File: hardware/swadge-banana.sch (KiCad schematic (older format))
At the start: 54 parts, among them J1 USB_B_Micro, SW1 SW_SPDT, SW2 4-1437565-2, SW3 4-1437565-2, SW4 4-1437565-2, U1 GS321-TR, U2 AP1117-33, U4 ESP-13-WROOM-02D, U5 BUS_PCIexpress, U6 DISP_OLED_UG-2864HSWEG01, U9 QMA6981

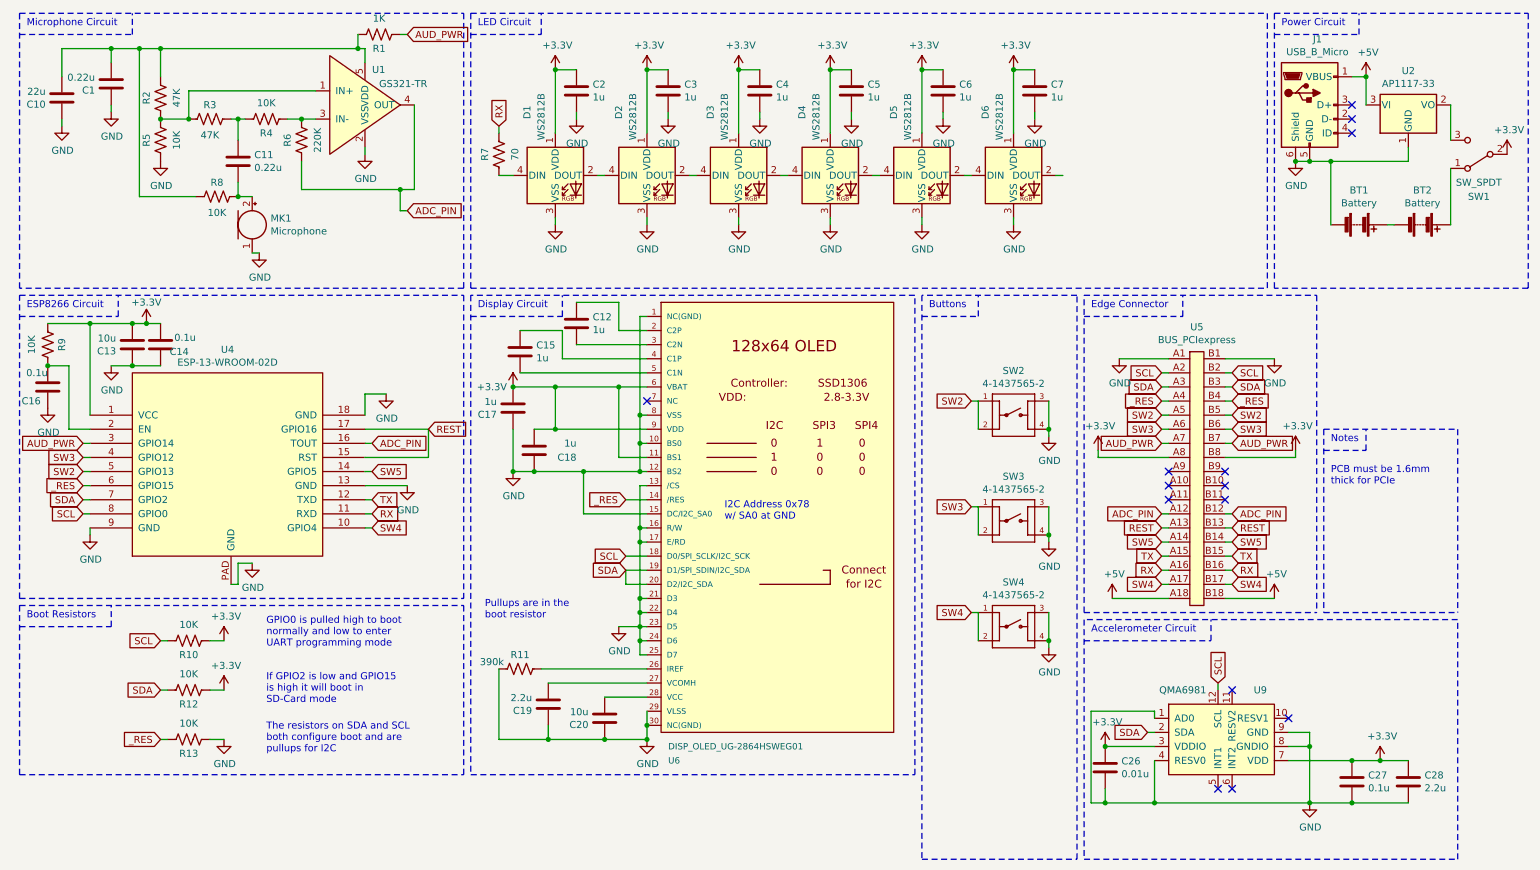
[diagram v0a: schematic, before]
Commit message: Reworked banana, started laying it out
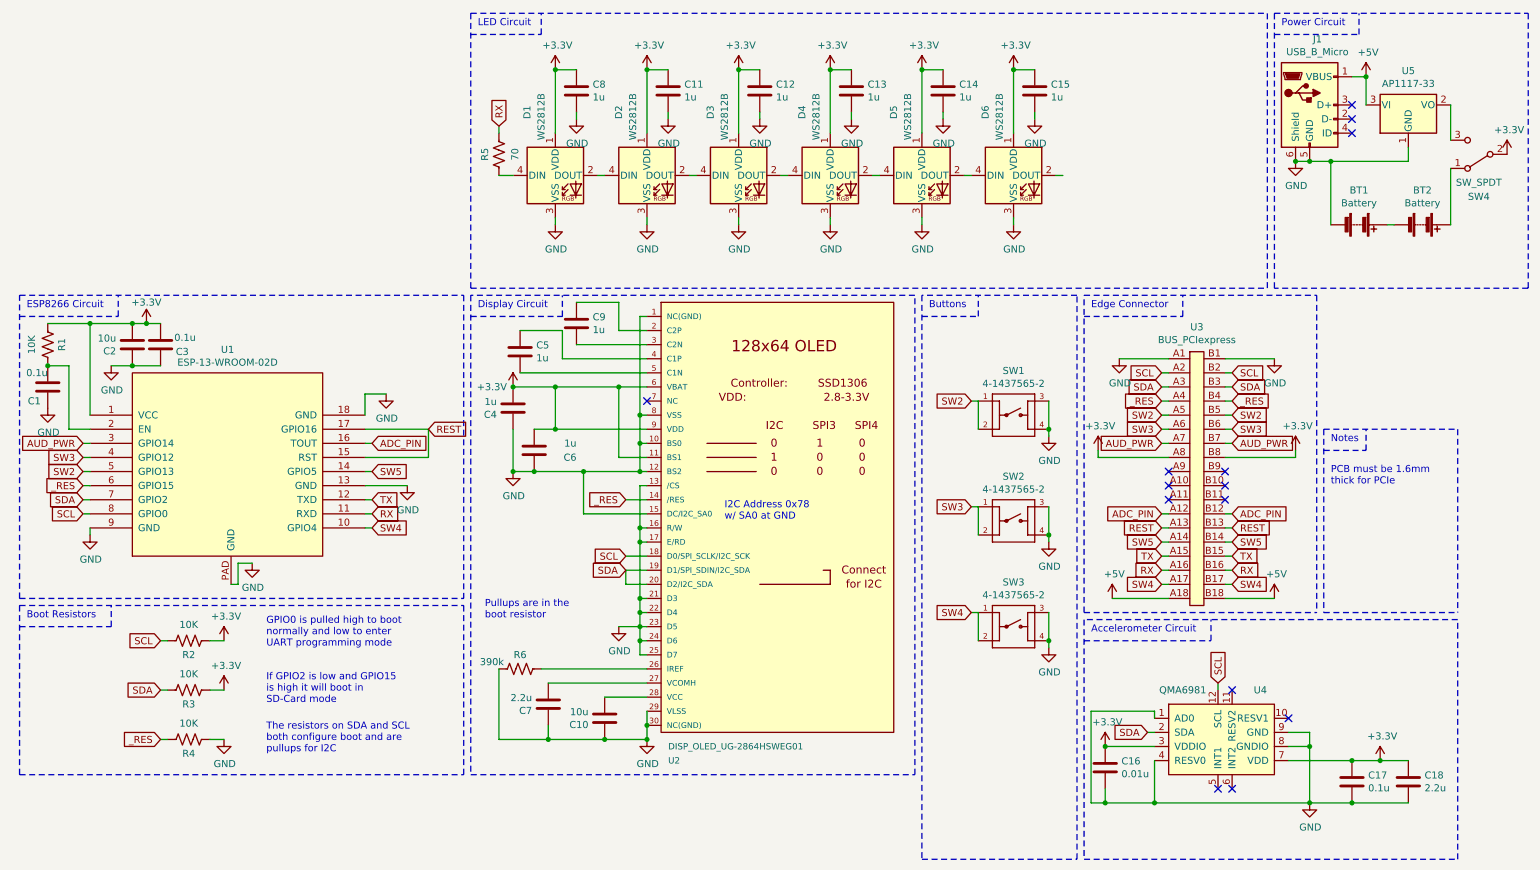
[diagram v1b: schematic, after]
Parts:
- removed C1, C11: 0.22u, Swadge_Parts:C_0603_1608Metric, symbol Swadge_Parts:C
- removed C10: 22u, Swadge_Parts:C_0603_1608Metric, symbol Swadge_Parts:C
- removed MK1: Microphone, Swadge_Parts:CMA-4544PF-W, symbol Swadge_Parts:Microphone
- removed R1: 1K, Swadge_Parts:R_0603_1608Metric, symbol Swadge_Parts:R_US
- removed R2, R3: 47K, Swadge_Parts:R_0603_1608Metric, symbol Swadge_Parts:R_US
- removed R4, R5, R8: 10K, Swadge_Parts:R_0603_1608Metric, symbol Swadge_Parts:R_US
- removed R6: 220K, Swadge_Parts:R_0603_1608Metric, symbol Swadge_Parts:R_US
- removed U1: GS321-TR, Swadge_Parts:SOT-23-5, symbol Swadge_Parts:GS321-TR
- C4: renamed from C17; footprint Swadge_Parts:C_0603_1608Metric -> Swadge_Parts:C_0805_2012Metric
- C5: renamed from C15; footprint Swadge_Parts:C_0603_1608Metric -> Swadge_Parts:C_0805_2012Metric
- C6: renamed from C18; footprint Swadge_Parts:C_0603_1608Metric -> Swadge_Parts:C_0805_2012Metric
- C9: renamed from C12; footprint Swadge_Parts:C_0603_1608Metric -> Swadge_Parts:C_0805_2012Metric
- U2: renamed from U6; footprint Swadge_Parts:microbuilder-UG-2864HSWEG01_0.96IN_WRAPAROUND -> Swadge_Parts:oled-flat
- renumbered C16 to C1, C20 to C10, C3 to C11, C4 to C12, C5 to C13, C6 to C14, C7 to C15, C26 to C16, C27 to C17, C28 to C18, C13 to C2, C14 to C3, C19 to C7, C2 to C8, R9 to R1, R10 to R2, R12 to R3, R13 to R4, R7 to R5, R11 to R6, SW2 to SW1, SW3 to SW2, SW4 to SW3, SW1 to SW4, U4 to U1, U5 to U3, U9 to U4, U2 to U5
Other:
- note removed: "Microphone Circuit"
